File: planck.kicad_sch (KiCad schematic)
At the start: 140 parts, among them J1 USB_C_U262-161N-4BVC11, J2 USB_C_U262-161N-4BVC11, J3 USB_C_U262-161N-4BVC11, SW1 SW_Hotswap_Kailh_Choc_V1_1u, SW10 SW_Hotswap_Kailh_Choc_V1_1u, SW11 SW_Hotswap_Kailh_Choc_V1_1u, SW12 SW_Hotswap_Kailh_Choc_V1_1u, SW13 SW_Hotswap_Kailh_Choc_V1_1u, SW14 SW_Hotswap_Kailh_Choc_V1_1u, SW15 SW_Hotswap_Kailh_Choc_V1_1u, SW16 SW_Hotswap_Kailh_Choc_V1_1u, SW17 SW_Hotswap_Kailh_Choc_V1_1u, SW18 SW_Hotswap_Kailh_Choc_V1_1u, SW19 SW_Hotswap_Kailh_Choc_V1_1u, SW2 SW_Hotswap_Kailh_Choc_V1_1u, SW20 SW_Hotswap_Kailh_Choc_V1_1u, SW21 SW_Hotswap_Kailh_Choc_V1_1u, SW22 SW_Hotswap_Kailh_Choc_V1_1u, SW23 SW_Hotswap_Kailh_Choc_V1_1u, SW24 SW_Hotswap_Kailh_Choc_V1_1u, SW25 SW_Push, SW26 DSHP02TSGET, SW3 SW_Hotswap_Kailh_Choc_V1_1u, SW4 SW_Hotswap_Kailh_Choc_V1_1u, SW5 SW_Hotswap_Kailh_Choc_V1_1u, SW6 SW_Hotswap_Kailh_Choc_V1_1u, SW7 SW_Hotswap_Kailh_Choc_V1_1u, SW8 SW_Hotswap_Kailh_Choc_V1_1u, SW9 SW_Hotswap_Kailh_Choc_V1_1u, U1 RP2040 ARM Cortex-M0 133MHz, U2 ME6219C33M5G, U3 W25Q16JVUXIQ, U5 tcase, Y1 32MHz ±10ppm 20pF SMD3225-4P

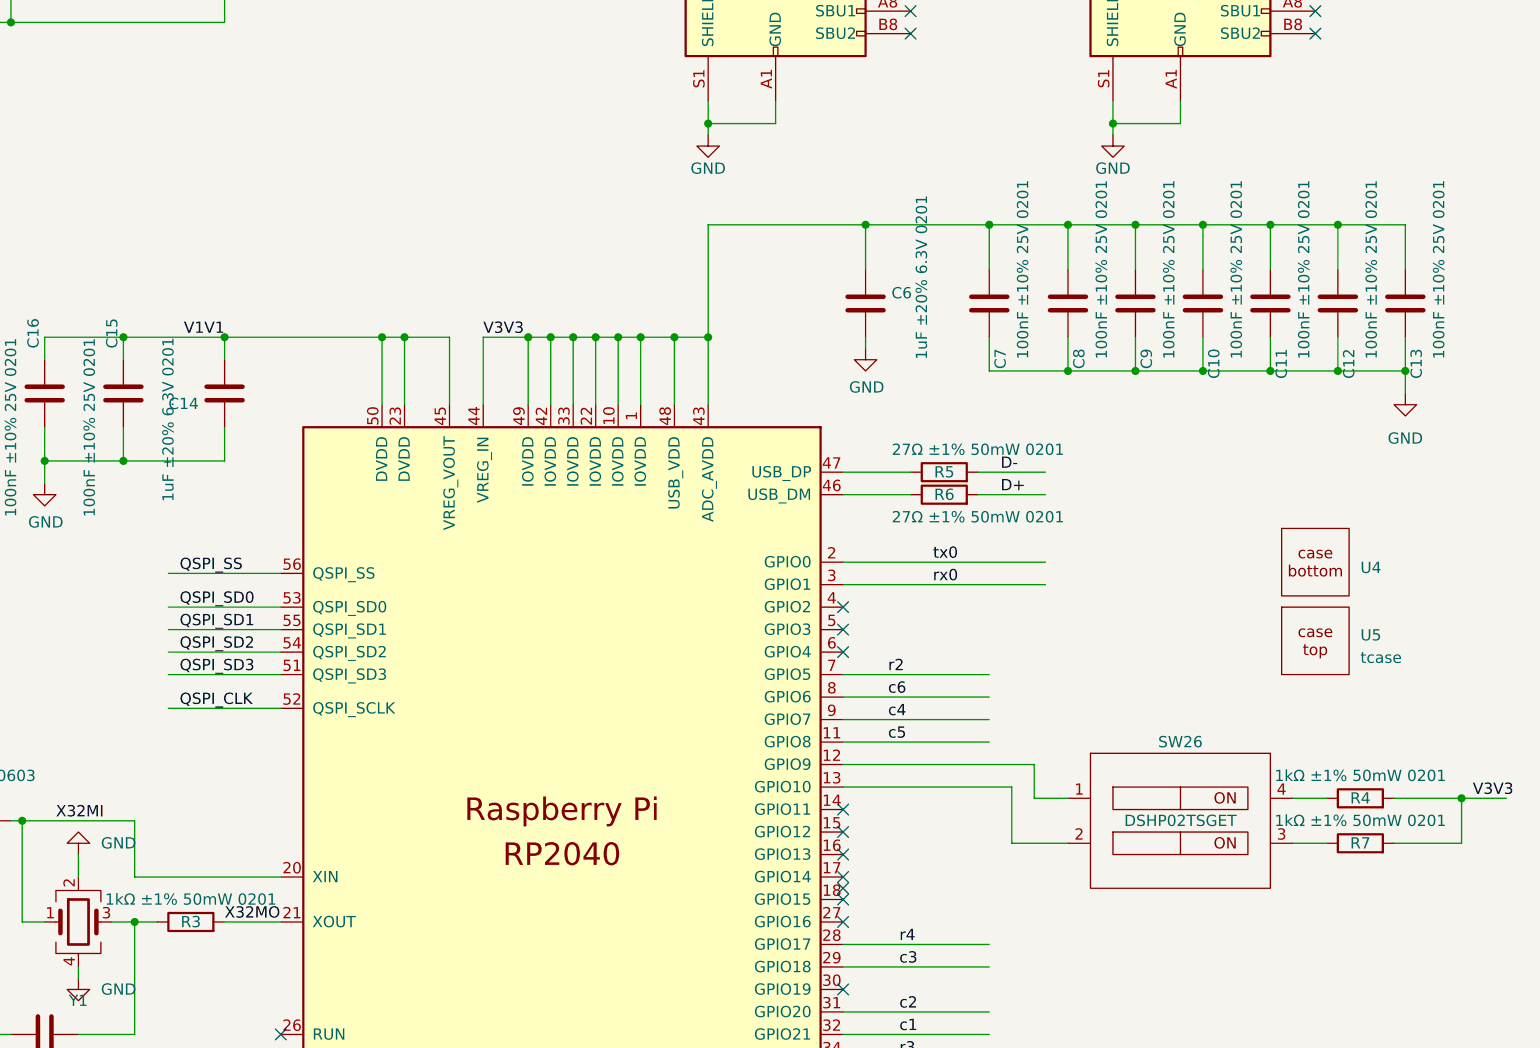
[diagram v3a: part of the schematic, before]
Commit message: distance check add serial resistor for protection
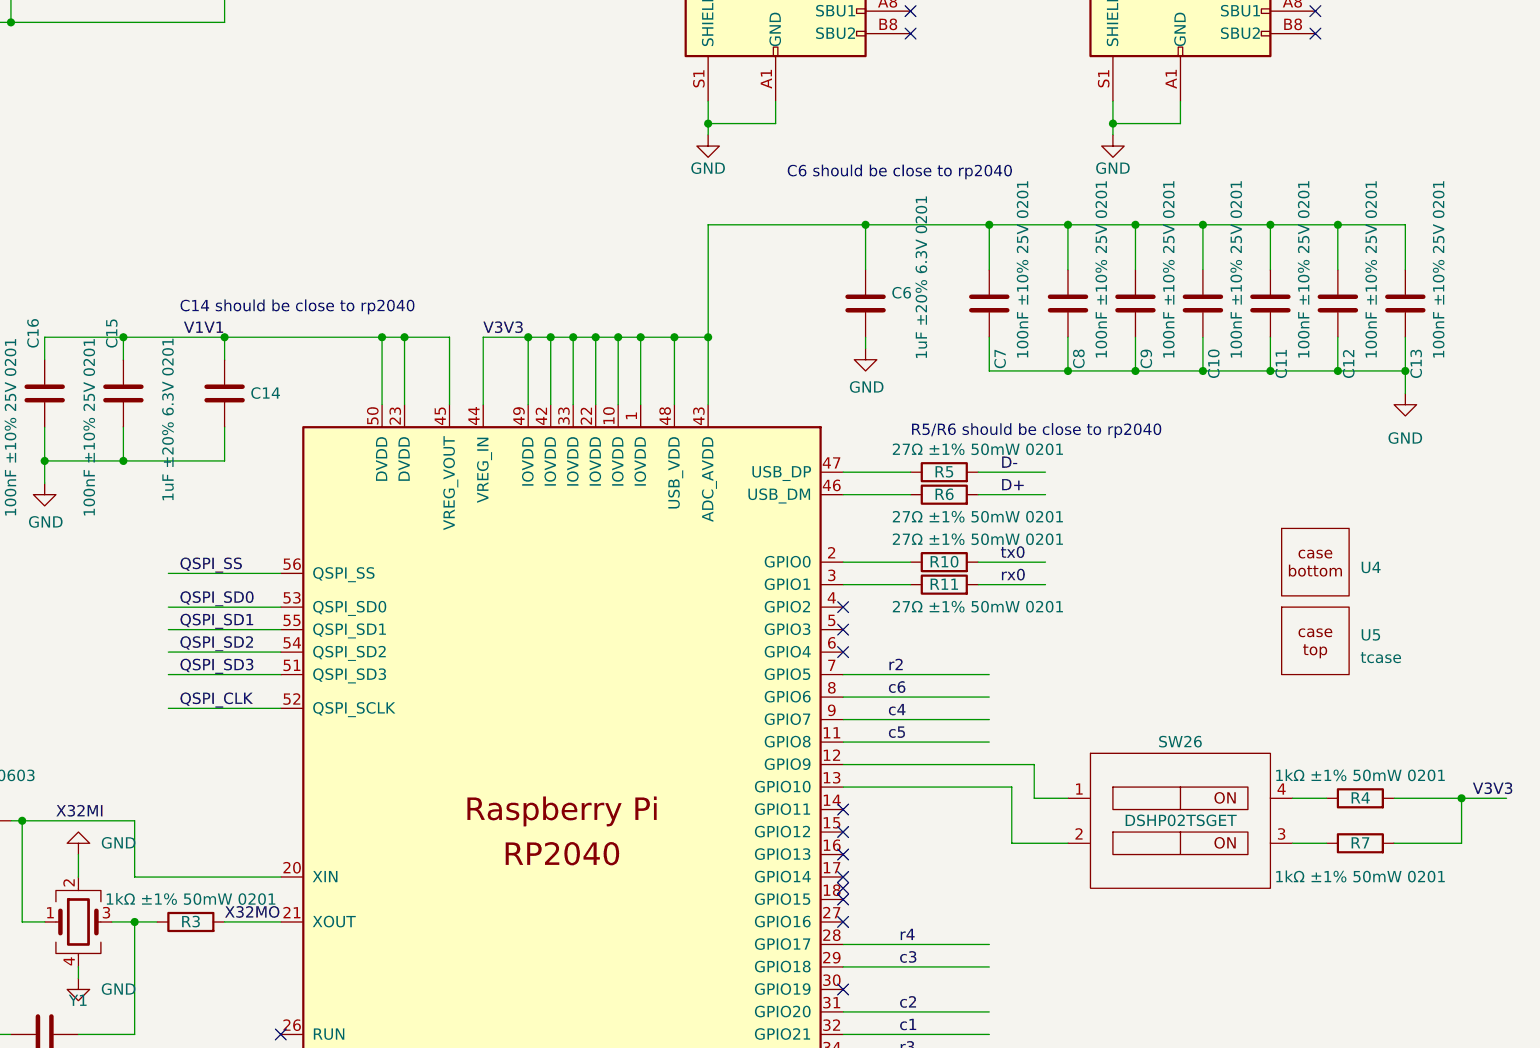
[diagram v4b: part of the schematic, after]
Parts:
- added R10, R11: 27Ω ±1% 50mW 0201, Resistor_SMD:R_0201_0603Metric, symbol Device:R
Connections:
- net rx0: now also R11.2; no longer U1.3 (GPIO1)
- net tx0: now also R10.2; no longer U1.2 (GPIO0)
- new net: R10.1, U1.2 (GPIO0)
- new net: R11.1, U1.3 (GPIO1)
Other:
- note added: "C14 should be close to rp2040"
- note added: "C6 should be close to rp2040"
- note added: "R5/R6 should be close to rp2040"
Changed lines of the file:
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@@
     (stroke (width 0) (type default))
   )
+  (wire (pts (xy 339.09 165.1) (xy 346.71 165.1))
+    (stroke (width 0) (type default))
+  )
   (wire (pts (xy 243.84 191.77) (xy 243.84 198.12))
     (stroke (width 0) (type default))
@@
     (stroke (width 0) (type default))
   )
+  (wire (pts (xy 323.85 162.56) (xy 331.47 162.56))
+    (stroke (width 0) (type default))
+  )
   (wire (pts (xy 68.58 115.57) (xy 68.58 105.41))
     (stroke (width 0) (type default))
@@
     (stroke (width 0) (type default))
   )
-  (wire (pts (xy 323.85 165.1) (xy 346.71 165.1))
-    (stroke (width 0) (type default))
-  )
   (wire (pts (xy 40.64 167.64) (xy 40.64 168.91))
     (stroke (width 0) (type default))
@@
     (stroke (width 0) (type default))
   )
-  (wire (pts (xy 323.85 162.56) (xy 346.71 162.56))
-    (stroke (width 0) (type default))
-  )
   (wire (pts (xy 383.54 92.71) (xy 377.19 92.71))
     (stroke (width 0) (type default))
@@
     (stroke (width 0) (type default))
   )
+  (wire (pts (xy 323.85 165.1) (xy 331.47 165.1))
+    (stroke (width 0) (type default))
+  )
   (wire (pts (xy 40.64 152.4) (xy 40.64 151.13))
     (stroke (width 0) (type default))
@@
     (stroke (width 0) (type default))
   )
+  (wire (pts (xy 339.09 162.56) (xy 346.71 162.56))
+    (stroke (width 0) (type default))
+  )
   (wire (pts (xy 40.64 190.5) (xy 40.64 191.77))
     (stroke (width 0) (type default))
@@
     (stroke (width 0) (type default))
   )
+  (text "R5/R6 should be close to rp2040" (at 331.47 148.59 0)
+    (effects (font (size 1.27 1.27)) (justify left bottom))
+  )
+  (text "C6 should be close to rp2040" (at 317.5 119.38 0)
+    (effects (font (size 1.27 1.27)) (justify left bottom))
+  )
+  (text "C14 should be close to rp2040" (at 248.92 134.62 0)
+    (effects (font (size 1.27 1.27)) (justify left bottom))
+  )
   (label "VBUS" (at 218.44 88.9 0) (fields_autoplaced)
     (effects (font (size 1.27 1.27)) (justify left bottom))
@@
     (effects (font (size 1.27 1.27)) (justify left bottom))
   )
-  (label "tx0" (at 334.01 162.56 0) (fields_autoplaced)
+  (label "tx0" (at 341.63 162.56 0) (fields_autoplaced)
     (effects (font (size 1.27 1.27)) (justify left bottom))
   )
@@
     (effects (font (size 1.27 1.27)) (justify left bottom))
   )
-  (label "rx0" (at 333.9875 165.1 0) (fields_autoplaced)
+  (label "rx0" (at 341.63 165.1 0) (fields_autoplaced)
     (effects (font (size 1.27 1.27)) (justify left bottom))
   )
@@
       (effects (font (size 1.27 1.27)))
     )
-    (property "Value" "1kΩ ±1% 50mW 0201" (at 382.27 191.77 90)
+    (property "Value" "1kΩ ±1% 50mW 0201" (at 382.27 198.12 90)
       (effects (font (size 1.27 1.27)))
     )
@@
   (symbol (lib_id "Device:C") (at 254 143.51 180) (unit 1)
     (in_bom yes) (on_board yes) (dnp no)
-    (property "Reference" "C14" (at 251.079 144.6784 0)
+    (property "Reference" "C14" (at 260.35 143.51 0)
       (effects (font (size 1.27 1.27)) (justify left))
     )
@@
     )
   )
+  (symbol (lib_id "Device:R") (at 335.28 165.1 90) (unit 1)
+    (in_bom yes) (on_board yes) (dnp no)
+    (property "Reference" "R11" (at 335.28 165.1 90)
+      (effects (font (size 1.27 1.27)))
+    )
+    (property "Value" "27Ω ±1% 50mW 0201" (at 339.09 167.64 90)
+      (effects (font (size 1.27 1.27)))
+    )
+    (property "Footprint" "Resistor_SMD:R_0201_0603Metric" (at 335.28 166.878 90)
+      (effects (font (size 1.27 1.27)) hide)
+    )
+    (property "Datasheet" "https://atta.szlcsc.com/upload/public/pdf/source/20200306/C422600_1E6D84923E4A46A82E41ADD87F860B5C.pdf" (at 335.28 165.1 0)
+      (effects (font (size 1.27 1.27)) hide)
+    )
+    (property "JLC" "C273268" (at 335.28 165.1 0)
+      (effects (font (size 1.27 1.27)) hide)
+    )
+    (pin "1")
+    (pin "2")
+    (instances
+      (project "planck"
+        (path "/27312bda-a56e-4031-ad08-90fe6bbef090"
+          (reference "R11") (unit 1)
+        )
+      )
+    )
+  )
   (symbol (lib_id "Diode:1N4148W") (at 132.08 121.92 180) (unit 1)
     (in_bom yes) (on_board yes) (dnp no)
@@
         )
       )
+    )
+  )
+  (symbol (lib_id "Device:R") (at 335.28 162.56 90) (unit 1)
+    (in_bom yes) (on_board yes) (dnp no)
+    (property "Reference" "R10" (at 335.28 162.56 90)
+      (effects (font (size 1.27 1.27)))
+    )
+    (property "Value" "27Ω ±1% 50mW 0201" (at 339.09 160.02 90)
+      (effects (font (size 1.27 1.27)))
+    )
+    (property "Footprint" "Resistor_SMD:R_0201_0603Metric" (at 335.28 164.338 90)
+      (effects (font (size 1.27 1.27)) hide)
+    )
+    (property "Datasheet" "https://atta.szlcsc.com/upload/public/pdf/source/20200306/C422600_1E6D84923E4A46A82E41ADD87F860B5C.pdf" (at 335.28 162.56 0)
+      (effects (font (size 1.27 1.27)) hide)
+    )
+    (property "JLC" "C273268" (at 335.28 162.56 0)
+      (effects (font (size 1.27 1.27)) hide)
+    )
+    (pin "1")
+    (pin "2")
+    (instances
+      (project "planck"
+        (path "/27312bda-a56e-4031-ad08-90fe6bbef090"
+          (reference "R10") (unit 1)
+        )
+      )
